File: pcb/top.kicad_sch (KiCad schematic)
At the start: 81 parts, among them J1 Conn_01x01, J10 Conn_01x01, J11 Conn_01x01, J2 Conn_01x01, J3 Conn_01x06, J4 Conn_01x01, J5 Conn_01x01, J6 Conn_01x01, J7 Conn_01x01, J8 Conn_01x01, J9 Conn_01x01, Q1 2N7002, Q2 2N7002, Q3 2N7002, Q4 2N7002, U1 L78L05_SOT89, U2 PIC12F629-ISN, U3 L78L08_SOT89

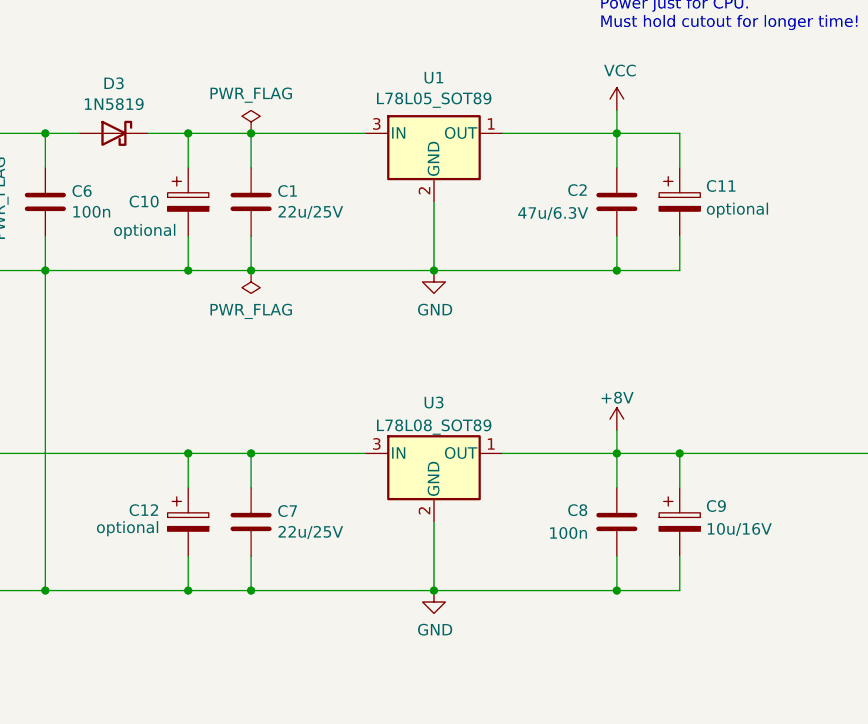
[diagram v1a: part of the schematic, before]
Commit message: Mark unused capacitors as DNP.
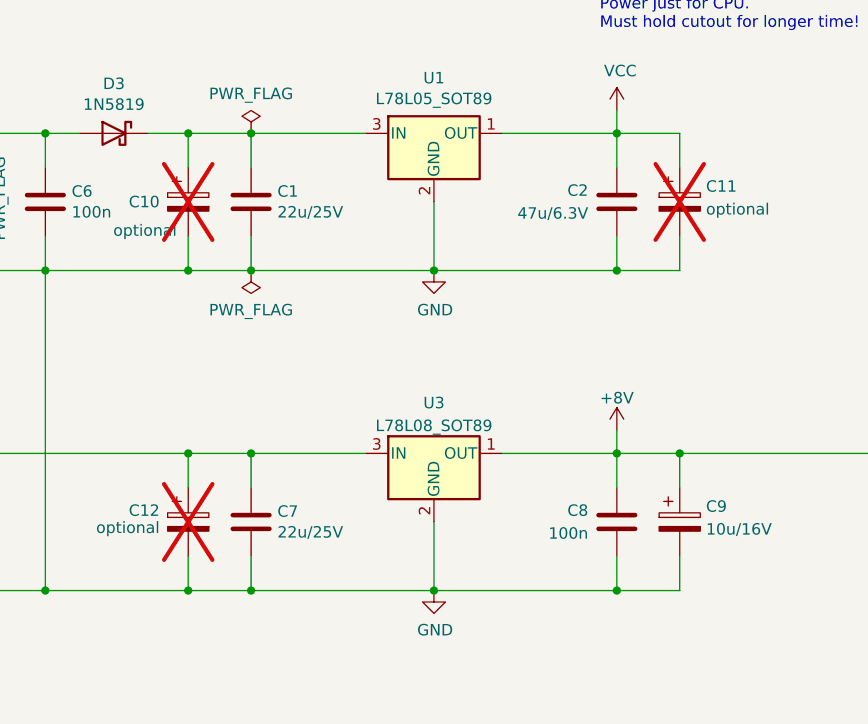
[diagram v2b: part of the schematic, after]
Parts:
- C10, C11, C12: now not fitted
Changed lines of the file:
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@@
   )
   (symbol (lib_id "Device:C_Polarized") (at 108.585 44.45 0) (unit 1)
-    (in_bom yes) (on_board yes) (dnp no)
+    (in_bom yes) (on_board yes) (dnp yes)
     (property "Reference" "C10" (at 105.41 44.45 0)
       (effects (font (size 1.27 1.27)) (justify right))
@@
   )
   (symbol (lib_id "Device:C_Polarized") (at 108.585 80.01 0) (unit 1)
-    (in_bom yes) (on_board yes) (dnp no)
+    (in_bom yes) (on_board yes) (dnp yes)
     (property "Reference" "C12" (at 105.41 78.74 0)
       (effects (font (size 1.27 1.27)) (justify right))
@@
   )
   (symbol (lib_id "Device:C_Polarized") (at 163.195 44.45 0) (unit 1)
-    (in_bom yes) (on_board yes) (dnp no) (fields_autoplaced)
+    (in_bom yes) (on_board yes) (dnp yes) (fields_autoplaced)
     (property "Reference" "C11" (at 166.116 42.7263 0)
       (effects (font (size 1.27 1.27)) (justify left))

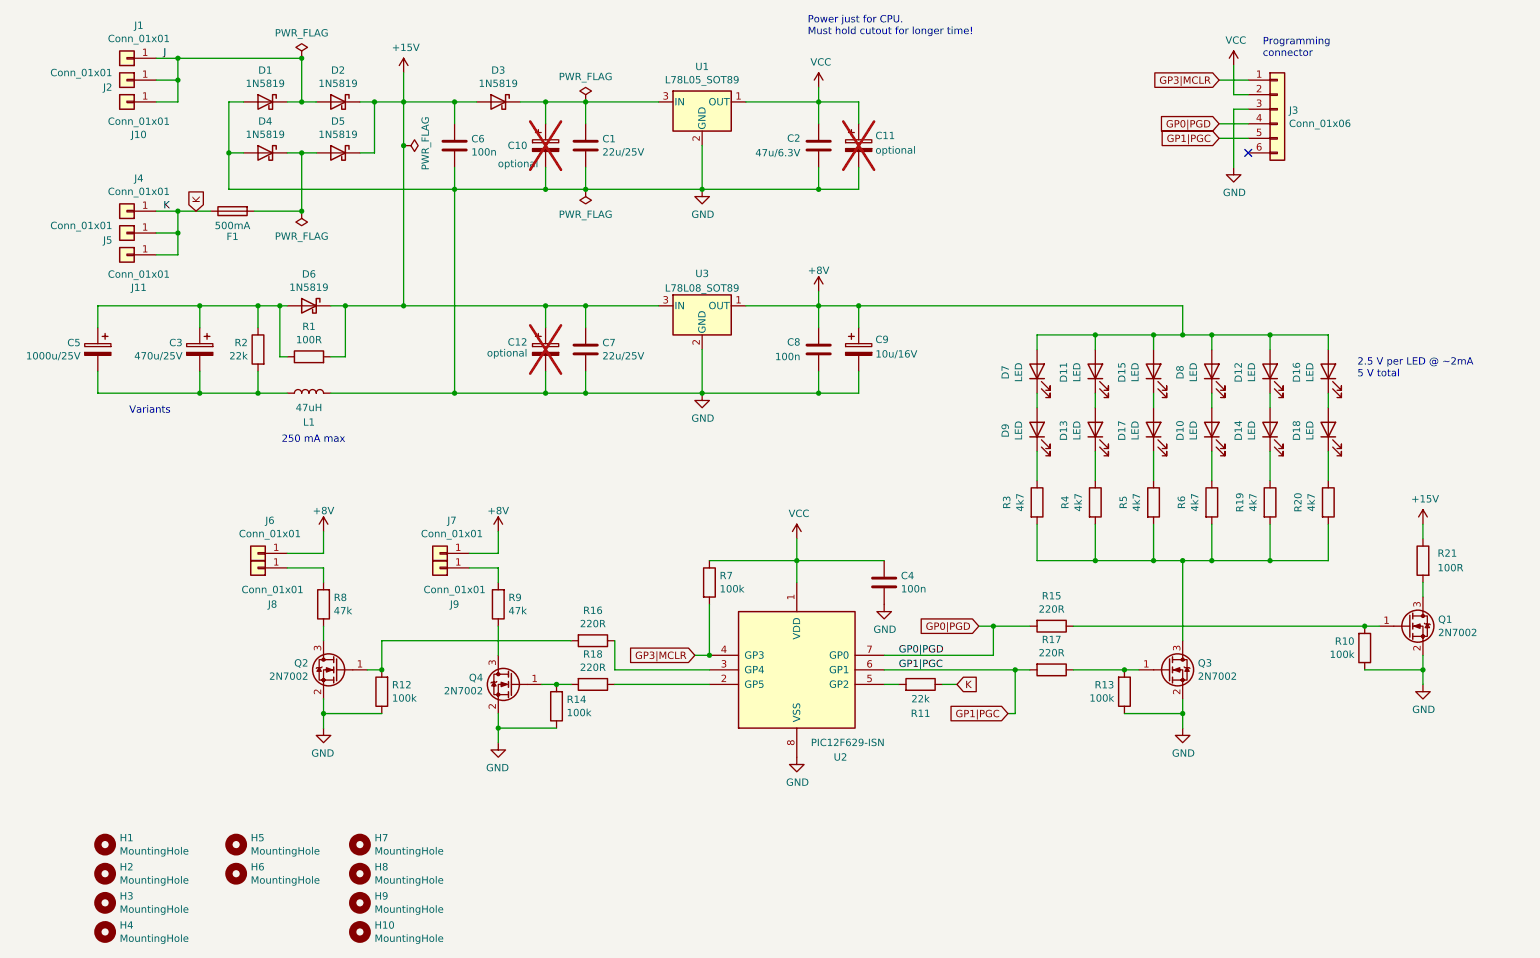
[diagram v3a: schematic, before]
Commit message: Connect CPU input after fuse.
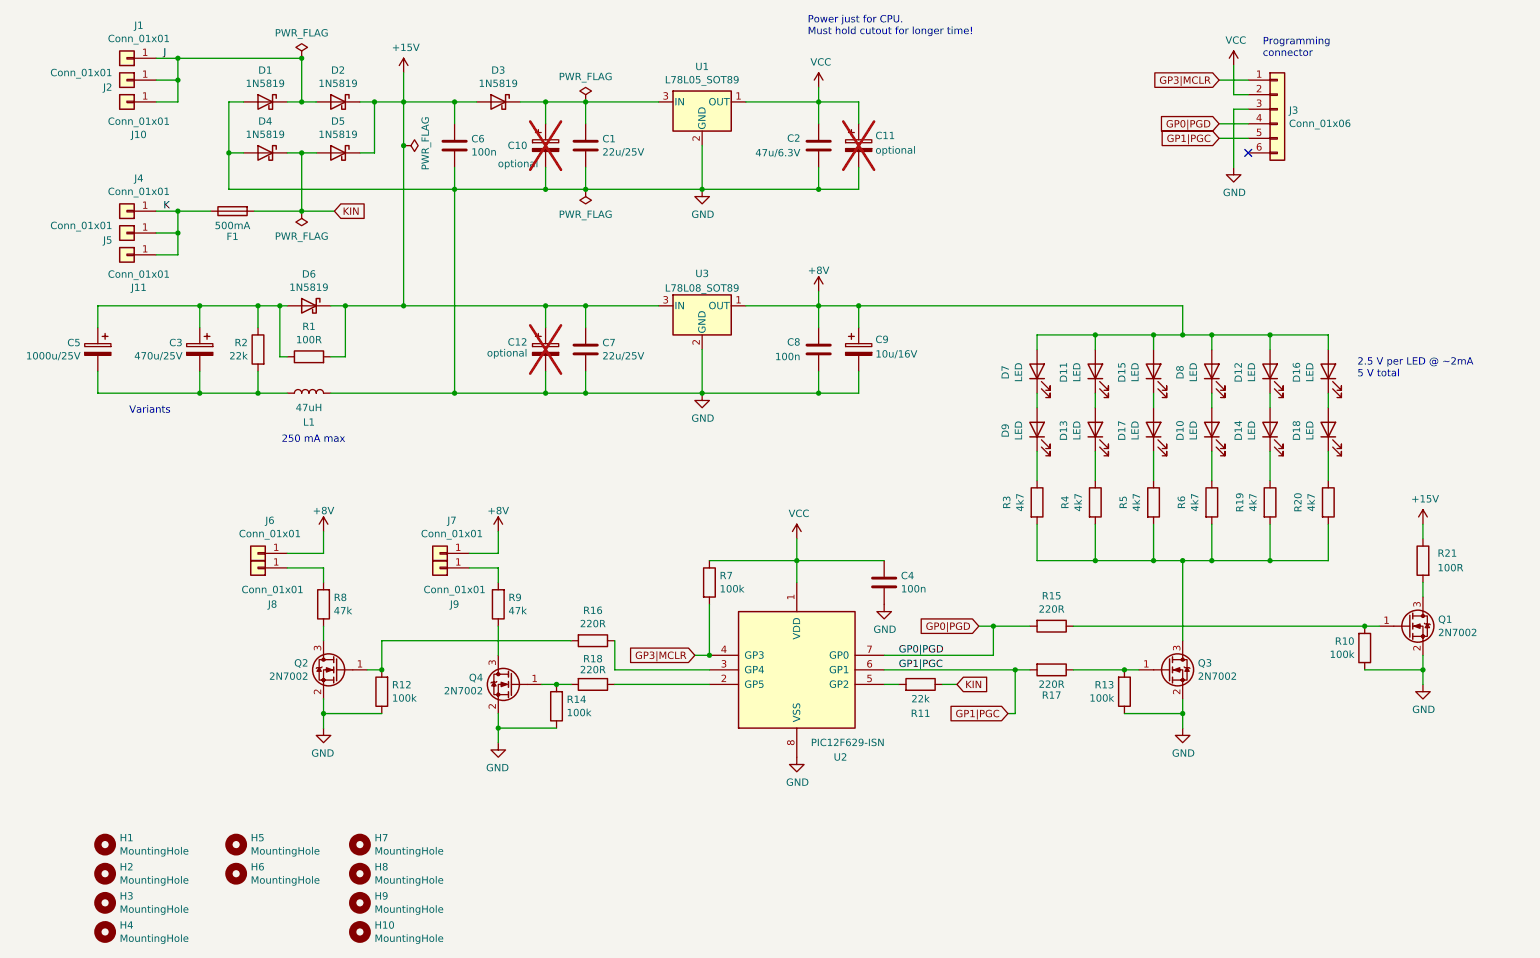
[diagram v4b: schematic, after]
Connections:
- net K: no longer R11.1
- net KIN: now reaches D4.1 (K), D5.2 (A), F1.2
- net KIN: now also R11.1
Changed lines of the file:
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@@
+    (stroke (width 0) (type default))
+  )
+  (wire (pts (xy 66.04 55.88) (xy 71.755 55.88))
     (stroke (width 0) (type default))
   )
@@
     )
   )
-  (global_label "K" (shape input) (at 47.625 55.88 90) (fields_autoplaced)
+  (global_label "KIN" (shape input) (at 71.755 55.88 0) (fields_autoplaced)
     (effects (font (size 1.27 1.27)) (justify left))
-    (property "Intersheetrefs" "${INTERSHEET_REFS}" (at -8.255 121.92 0)
-      (effects (font (size 1.27 1.27)) hide)
+    (property "Intersheetrefs" "${INTERSHEET_REFS}" (at 77.2913 55.88 0)
+      (effects (font (size 1.27 1.27)) (justify left) hide)
     )
   )
@@
     )
   )
-  (global_label "K" (shape input) (at 180.34 138.43 0) (fields_autoplaced)
+  (global_label "KIN" (shape input) (at 180.34 138.43 0) (fields_autoplaced)
     (effects (font (size 1.27 1.27)) (justify left))
-    (property "Intersheetrefs" "${INTERSHEET_REFS}" (at 183.941 138.43 0)
+    (property "Intersheetrefs" "${INTERSHEET_REFS}" (at 185.8763 138.43 0)
       (effects (font (size 1.27 1.27)) (justify left) hide)
     )
@@
   (symbol (lib_id "Device:R") (at 196.85 135.89 270) (unit 1)
     (in_bom yes) (on_board yes) (dnp no)
-    (property "Reference" "R17" (at 196.85 130.6322 90)
-      (effects (font (size 1.27 1.27)))
-    )
-    (property "Value" "220R" (at 196.85 132.9436 90)
+    (property "Reference" "R17" (at 196.85 140.335 90)
+      (effects (font (size 1.27 1.27)))
+    )
+    (property "Value" "220R" (at 196.85 138.43 90)
       (effects (font (size 1.27 1.27)))
     )
@@
   (symbol (lib_id "Device:R") (at 116.84 138.43 270) (unit 1)
     (in_bom yes) (on_board yes) (dnp no)
-    (property "Reference" "R18" (at 116.84 133.1722 90)
-      (effects (font (size 1.27 1.27)))
-    )
-    (property "Value" "220R" (at 116.84 135.4836 90)
-      (effects (font (size 1.27 1.27)))
-    )
+    (property "Reference" "R18" (at 116.84 133.985 90)
+      (effects (font (size 1.27 1.27)))
+    )
+    (property "Value" "220R" (at 116.84 135.89 90)
+      (effects (font (size 1.27 1.27)))
+    )

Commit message: sch: update interior LEDs current, add notes.
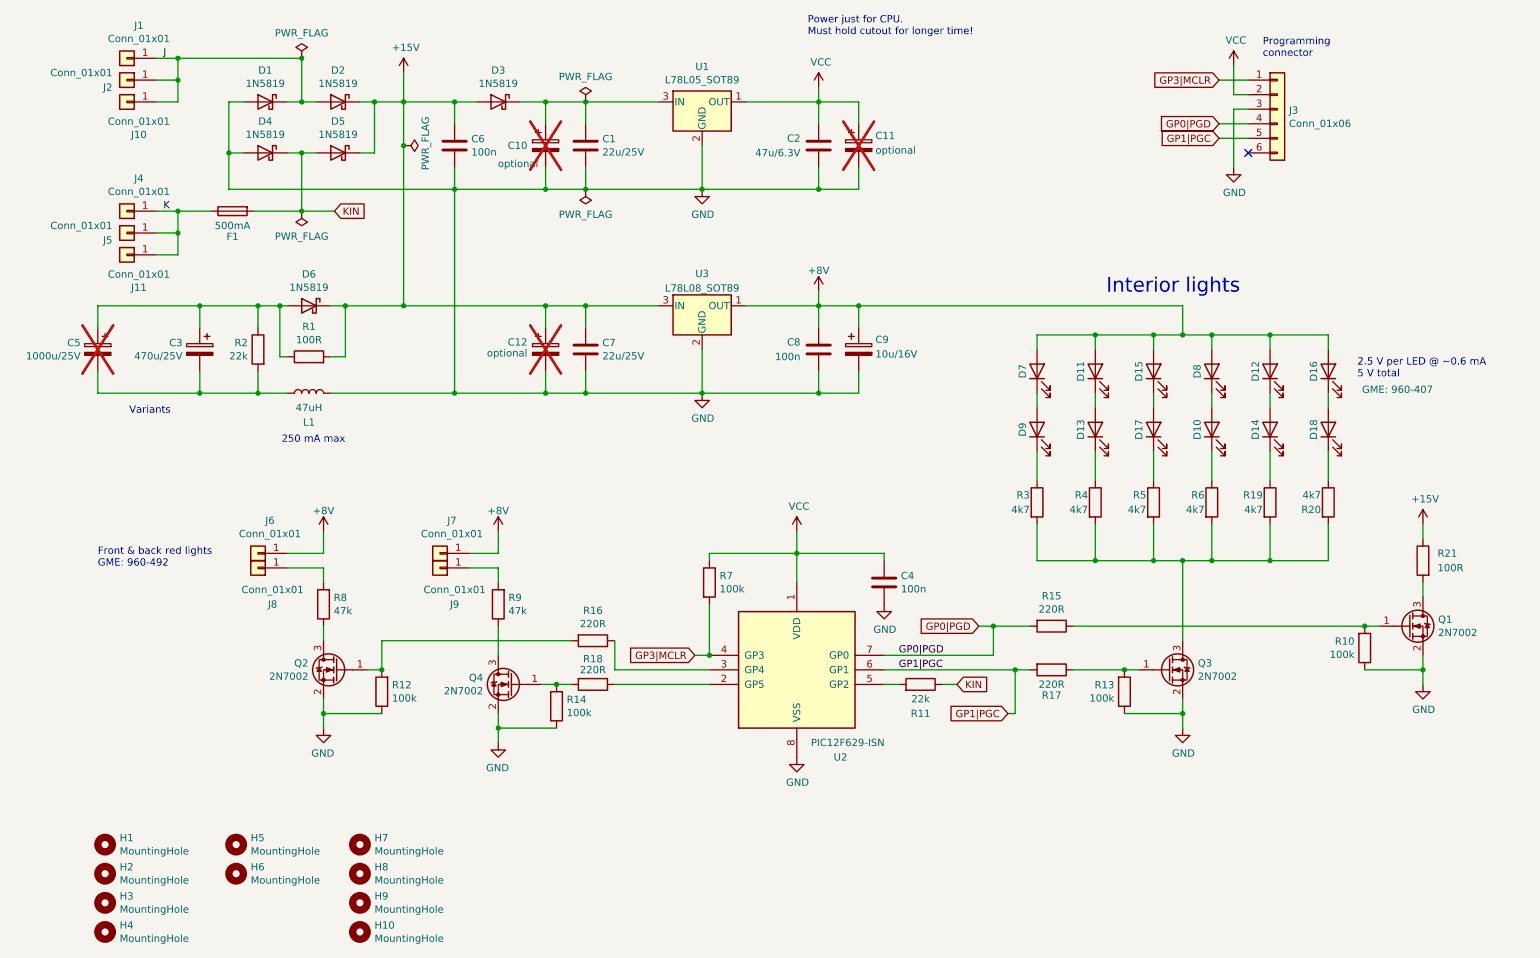
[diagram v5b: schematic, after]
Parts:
- C5: now not fitted
- D10, D11, D12, D13, D14, D15, D16, D17, D18, D7, D8, D9: GME (none) -> 960-407
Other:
- note added: "2.5 V per LED @ ~0.6 mA 5 V total"
- note added: "Front & back red lights GME: 960-492"
- note added: "Interior lights"
- note removed: "2.5 V per LED @ ~2mA 5 V total"

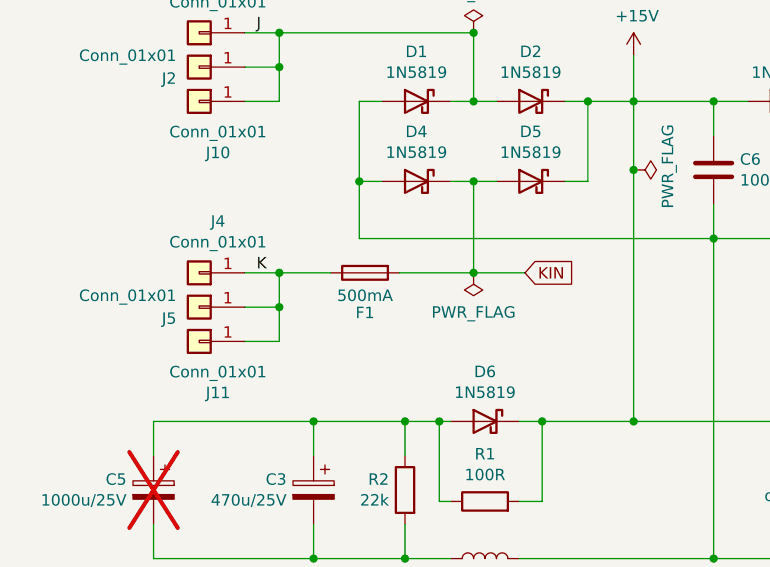
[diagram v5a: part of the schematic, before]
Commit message: F1: fuse -> polyfuse, 500mA -> 300mA.
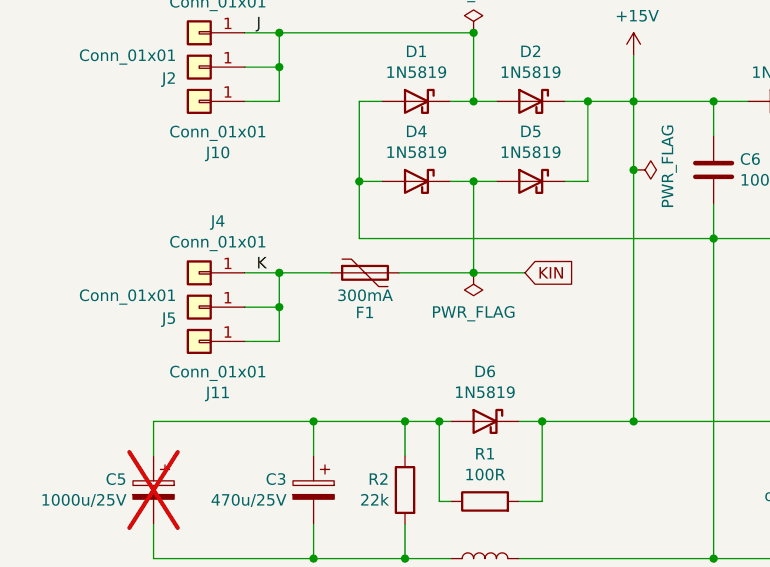
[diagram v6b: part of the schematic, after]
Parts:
- F1: value 500mA -> 300mA; symbol Device:Fuse -> Device:Polyfuse; LCSC C136341 -> C151132
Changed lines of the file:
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@@
     )
   )
-  (symbol (lib_id "Device:Fuse") (at 53.975 55.88 90) (mirror x) (unit 1)
+  (symbol (lib_id "Device:Polyfuse") (at 53.975 55.88 90) (mirror x) (unit 1)
     (in_bom yes) (on_board yes) (dnp no)
     (property "Reference" "F1" (at 53.975 60.325 90)
       (effects (font (size 1.27 1.27)))
     )
-    (property "Value" "500mA" (at 53.975 58.42 90)
+    (property "Value" "300mA" (at 53.975 58.42 90)
       (effects (font (size 1.27 1.27)))
     )
-    (property "Footprint" "Fuse:Fuse_1206_3216Metric_Pad1.42x1.75mm_HandSolder" (at 53.975 54.102 90)
-      (effects (font (size 1.27 1.27)) hide)
+    (property "Footprint" "Fuse:Fuse_1206_3216Metric_Pad1.42x1.75mm_HandSolder" (at 59.055 57.15 0)
+      (effects (font (size 1.27 1.27)) (justify left) hide)
     )
     (property "Datasheet" "~" (at 53.975 55.88 0)
       (effects (font (size 1.27 1.27)) hide)
     )
-    (property "LCSC" "C136341" (at 53.975 55.88 0)
+    (property "LCSC" "C151132" (at 53.975 55.88 0)
       (effects (font (size 1.27 1.27)) hide)
     )
